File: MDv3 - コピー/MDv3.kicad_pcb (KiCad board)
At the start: 2 copper layers, 59.3 x 76.1 mm, 46 parts, among them J1 XT60PW-M, J2 XT60PW-M, J3 XT30PW-M, J4 XT30PW-M

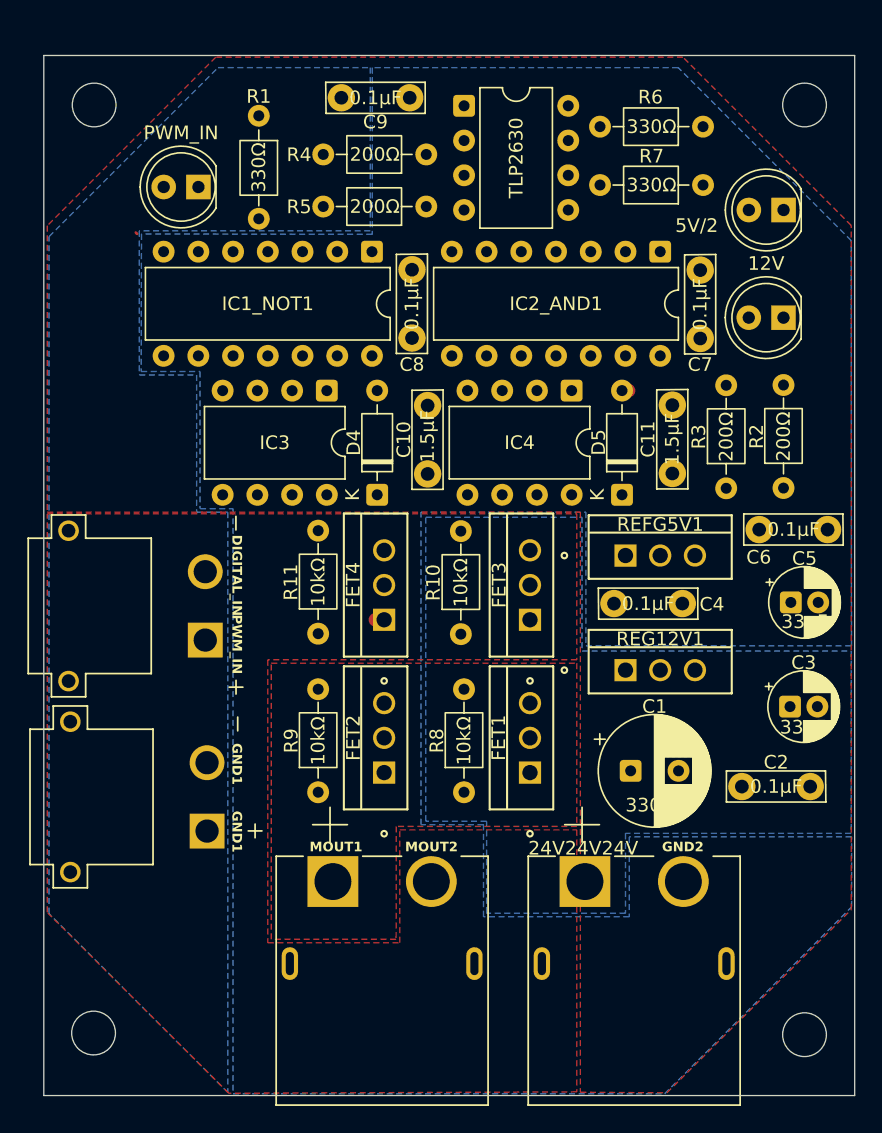
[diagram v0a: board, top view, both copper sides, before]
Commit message: 不要な塗りつぶしを削除、二層にして横向きXTにするということは基盤を大きくしてもいいということだ。
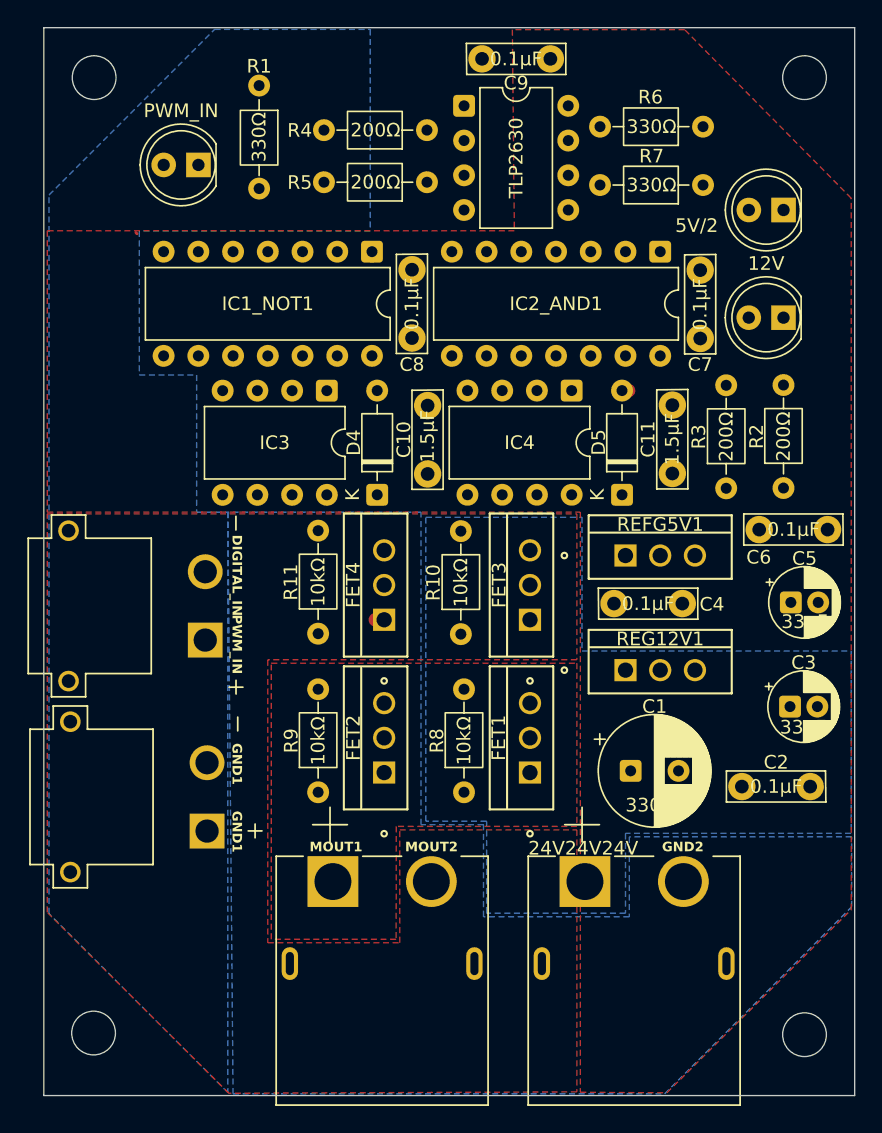
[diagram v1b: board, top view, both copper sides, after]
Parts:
- moved C9 10.7 mm to (123.4, 111.7)
- moved R1 2.21 mm to (102.1, 113.6)
- moved REF** 2.00 mm to (142.0, 113.0)
- moved REF** 2.00 mm to (90.0, 113.0)
- moved R4 1.78 mm to (114.4, 116.9)
- moved R5 1.78 mm to (114.4, 120.7)
- moved D1 1.61 mm to (97.7, 119.4)
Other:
- board size 59.3 x 76.1 mm -> 59.3 x 78.1 mm
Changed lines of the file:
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@@
 	(footprint "Library:R_Axial_DIN0207_L6.3mm_D2.5mm_P10.16mm_Horizontal_kai"
 		(layer "F.Cu")
-		(at 114.3 122.452 180)
+		(at 114.3502 120.674 180)
 		(property "Reference" "R5"
 			(at 7 -2.25 180)
@@
 	(footprint "MountingHole:MountingHole_3.2mm_M3"
 		(layer "F.Cu")
-		(at 142 115)
+		(at 142 113)
 		(descr "Mounting Hole 3.2mm, M3, no annular, generated by kicad-footprint-generator mountinghole.py")
 		(tags "mountinghole M3")
@@
 	(footprint "MountingHole:MountingHole_3.2mm_M3"
 		(layer "F.Cu")
-		(at 90.043 115)
+		(at 90.043 113)
 		(descr "Mounting Hole 3.2mm, M3, no annular, generated by kicad-footprint-generator mountinghole.py")
 		(tags "mountinghole M3")
@@
 	(footprint "Library:R_Axial_DIN0207_L6.3mm_D2.5mm_P10.16mm_Horizontal_kai"
 		(layer "F.Cu")
-		(at 102.108 115.824 -90)
+		(at 102.132 113.6148 -90)
 		(property "Reference" "R1"
 			(at 7 -2.25 270)
@@
 	(footprint "LED_THT:LED_D5.0mm"
 		(layer "F.Cu")
-		(at 97.668 121 180)
+		(at 97.668 119.385 180)
 		(descr "LED, diameter 5.0mm, 2 pins, http://cdn-reichelt.de/documents/datenblatt/A500/LL-504BC2E-009.pdf, generated by kicad-footprint-generator")
 		(tags "LED")
@@
 	(footprint "Library:C_Disc_D11.0mm_W5.0mm_P5.0mm_kai"
 		(layer "F.Cu")
-		(at 113.1295 114.5165 180)
+		(at 123.4165 111.6705 180)
 		(property "Reference" "C9"
 			(at 5 -2 180)
@@
 	(footprint "Library:R_Axial_DIN0207_L6.3mm_D2.5mm_P10.16mm_Horizontal_kai"
 		(layer "F.Cu")
-		(at 114.3 118.642 180)
+		(at 114.3502 116.864 180)
 		(property "Reference" "R4"
 			(at 7 -2.25 180)
@@
 	)
 	(gr_rect
-		(start 86.36 111.379)
+		(start 86.36 109.347)
 		(end 145.669 187.452)
 		(stroke
@@
 		(polygon
 			(pts
-				(xy 125.603 187.211026) (xy 131.930282 187.251586) (xy 145.415 173.853031) (xy 145.415 123.814)
-				(xy 133.107 111.506) (xy 98.931 111.506) (xy 86.614 123.823) (xy 86.614 144.78) (xy 125.603 144.78)
+				(xy 125.603 187.211026) (xy 131.930282 187.251586) (xy 145.415 173.853031) (xy 145.415 121.815466)
+				(xy 133.232197 109.492) (xy 120.631182 109.492) (xy 120.777 124.206) (xy 86.614 124.20018) (xy 86.614 144.78)
+				(xy 125.603 144.78)
 			)
 		)
@@
 			(pts
 				(xy 110.236 124.206) (xy 93.345 124.206) (xy 93.345 134.747) (xy 97.536 134.747) (xy 97.536 144.78)
-				(xy 99.822 144.78) (xy 99.822 187.071) (xy 99.822 187.22975) (xy 86.741 174.14875) (xy 86.741 124.634)
-				(xy 99.107 112.268) (xy 110.236 112.268)
+				(xy 99.822 144.78) (xy 99.822 187.071) (xy 99.822 187.22975) (xy 86.741 174.14875) (xy 86.741 121.586)
+				(xy 98.853 109.474) (xy 110.236 109.474)
 			)
 		)
@@
 			(pts
 				(xy 129.185597 168.529725) (xy 129.185597 174.371725) (xy 118.517597 174.371725) (xy 118.517597 167.640725)
-				(xy 113.945597 167.640725) (xy 113.945597 144.780725) (xy 126.010597 144.780725) (xy 126.010597 154.559725)
-				(xy 145.434879 154.559725) (xy 145.416101 124.916419) (xy 132.759602 112.26822) (xy 110.389597 112.268725)
-				(xy 110.389597 124.46) (xy 93.505341 124.434828) (xy 93.47872 134.493) (xy 97.79 134.493) (xy 97.79 144.526)
-				(xy 100.203 144.526344) (xy 100.203 187.324943) (xy 131.769052 187.325617) (xy 145.441597 173.653363)
-				(xy 145.441597 168.529725)
+				(xy 113.945597 167.640725) (xy 113.945597 144.780725) (xy 99.822 144.78) (xy 100.203 187.324943)
+				(xy 131.769052 187.325617) (xy 145.441597 173.653363) (xy 145.441597 168.529725)
 			)
 		)

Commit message: ようはこういうことですよね
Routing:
- net +5V/2: track 0.67 -> 126.9 mm
- net +12V: track 0.60 -> 73.8 mm
- net PWM_NOT: track 0.00 -> 26.4 mm, vias 0 -> 1
- net DIGITAL_NOT: track 0.51 -> 23.9 mm
- net Net-(D2-A): track 0.00 -> 21.9 mm
- net Net-(D4-K): track 0.01 -> 8.01 mm
- net Net-(D1-A): track 0.00 -> 7.70 mm
- net Net-(D3-A): track 0.00 -> 5.63 mm
- net Net-(R4-Pad1): track 0.00 -> 3.03 mm
- net Net-(R5-Pad1): track 0.48 -> 3.40 mm

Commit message: 一旦詰み
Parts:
- moved C10 0.64 mm to (113.8, 142.0)
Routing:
- net PWM_IN: track 0.00 -> 68.2 mm, vias 0 -> 2
- net GND1: track 0.00 -> 59.0 mm, vias 0 -> 1
- net DIGITAL_IN: track 0.13 -> 54.4 mm
- net PWM1: track 0.00 -> 33.9 mm
- net DIGITAL: track 0.00 -> 26.7 mm, vias 0 -> 2
- net MOUT2: track 0.01 -> 15.2 mm
- net MOUT1: track 0.00 -> 14.5 mm
- net GATE2: track 0.00 -> 12.4 mm, vias 0 -> 3
- net Net-(D5-K): track 0.00 -> 8.01 mm
- net Net-(D1-A): track 7.70 -> 10.8 mm
- net +12V: track 73.8 -> 76.7 mm
- net +5V/2: track 126.9 -> 125.9 mm
- net PWM_NOT: track 26.4 -> 25.5 mm, vias 1 -> 0
- net Net-(D4-K): track 8.01 -> 7.35 mm

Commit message: 無理矢理完成
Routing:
- net Net-(FET1-G): track 0.00 -> 57.4 mm, vias 0 -> 12
- net Net-(FET2-G): track 0.00 -> 33.0 mm, vias 0 -> 3
- net MOUT1: track 14.5 -> 42.3 mm, vias 0 -> 4
- net GATE1: track 0.00 -> 22.4 mm, vias 0 -> 4
- net Net-(FET3-G): track 0.00 -> 18.7 mm
- net Net-(FET4-G): track 0.63 -> 19.0 mm
- net MOUT2: track 15.2 -> 19.3 mm

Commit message: いや無理じゃね？
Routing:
- net Net-(FET1-G): track 57.4 -> 59.0 mm
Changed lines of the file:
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@@
+	)
+	(segment
+		(start 113.99813 153.97187)
+		(end 113.9952 153.9748)
+		(width 1)
+		(layer "F.Cu")
+		(net 6)
+	)
+	(segment
+		(start 112.906257 151.229374)
+		(end 113.99813 152.321247)
+		(width 1)
+		(layer "F.Cu")
+		(net 6)
 	)
 	(segment
@@
 	)
 	(segment
-		(start 113.9952 153.9748)
+		(start 112.906257 150.2156)
+		(end 112.906257 151.229374)
+		(width 1)
+		(layer "F.Cu")
+		(net 6)
+	)
+	(segment
+		(start 113.99813 152.321247)
 		(end 113.99813 153.97187)
 		(width 1)
@@
 		(net 6)
 	)
-	(segment
-		(start 113.99813 153.97187)
-		(end 113.99813 152.321247)
-		(width 1)
-		(layer "F.Cu")
-		(net 6)
-	)
-	(segment
-		(start 113.99813 152.321247)
-		(end 112.9696 151.292717)
-		(width 1)
-		(layer "F.Cu")
-		(net 6)
-	)
-	(via
-		(at 112.9696 151.292717)
+	(via
+		(at 112.906257 150.2156)
 		(size 0.6)
 		(drill 0.3)
@@
 	)
 	(segment
-		(start 112.906257 151.229374)
-		(end 112.9696 151.292717)
-		(width 0.2)
-		(layer "B.Cu")
-		(net 6)
-	)
-	(segment
 		(start 104.399 141.097)
 		(end 101.981 143.515)
@@
 	)
 	(segment
+		(start 112.906257 146.848472)
+		(end 112.906257 150.2156)
+		(width 1)
+		(layer "B.Cu")
+		(net 6)
+	)
+	(segment
 		(start 109.655 141.097)
 		(end 110.0995 140.6525)
@@
 	)
 	(segment
-		(start 112.906257 146.848472)
-		(end 112.906257 151.229374)
-		(width 1)
-		(layer "B.Cu")
-		(net 6)
-	)
-	(segment
 		(start 114.503078 140.2525)
 		(end 110.4995 140.2525)
@@
 	)
 	(segment
-		(start 104.3432 161.6456)
+		(start 104.3148 164.4396)
 		(end 104.3432 164.468)
-		(width 0.6)
+		(width 0.2)
 		(layer "F.Cu")
 		(net 13)
@@
 	)
 	(segment
+		(start 102.273 159.7152)
+		(end 102.274 159.7162)
+		(width 0.6)
+		(layer "F.Cu")
+		(net 13)
+	)
+	(segment
+		(start 102.274 159.7162)
+		(end 102.274 164.4396)
+		(width 0.6)
+		(layer "F.Cu")
+		(net 13)
+	)
+	(segment
 		(start 97.7392 141.5796)
 		(end 97.7392 144.6276)
@@
 	)
 	(segment
-		(start 103.5812 160.8836)
-		(end 104.3432 161.6456)
-		(width 0.6)
-		(layer "F.Cu")
-		(net 13)
-	)
-	(segment
 		(start 111.1504 166.624)
 		(end 113.538 166.624)
@@
 	)
 	(segment
+		(start 102.273 158.8516)
+		(end 102.273 159.7152)
+		(width 0.6)
+		(layer "F.Cu")
+		(net 13)
+	)
+	(segment
+		(start 102.274 164.4396)
+		(end 104.3148 164.4396)
+		(width 0.6)
+		(layer "F.Cu")
+		(net 13)
+	)
+	(segment
 		(start 120.482 165.268)
 		(end 121.92 163.83)
@@
 	)
 	(via
-		(at 103.5812 160.8836)
-		(size 0.6)
-		(drill 0.3)
-		(layers "F.Cu" "B.Cu")
-		(net 13)
-	)
-	(via
 		(at 95.955386 152.863014)
 		(size 0.6)
@@
 	(via
 		(at 95.9612 148.298)
+		(size 0.6)
+		(drill 0.3)
+		(layers "F.Cu" "B.Cu")
+		(net 13)
+	)
+	(via
+		(at 102.273 158.8516)
 		(size 0.6)
 		(drill 0.3)
@@
 	)
 	(segment
-		(start 95.981219 155.468019)
-		(end 101.3968 160.8836)
-		(width 0.6)
-		(layer "B.Cu")
-		(net 13)
-	)
-	(segment
 		(start 104.3432 164.468)
 		(end 104.3432 166.068)
@@
 	)
 	(segment
-		(start 95.981219 154.929283)
-		(end 95.981219 155.468019)
-		(width 0.6)
-		(layer "B.Cu")
-		(net 13)
-	)
-	(segment
-		(start 101.3968 160.8836)
-		(end 103.5812 160.8836)
+		(start 102.273 158.8516)
+		(end 99.3648 158.8516)
 		(width 0.6)
 		(layer "B.Cu")
@@
 	)
 	(segment
+		(start 99.3648 158.8516)
+		(end 95.981219 155.468019)
+		(width 0.6)
+		(layer "B.Cu")
+		(net 13)
+	)
+	(segment
 		(start 114.9956 165.268)
 		(end 117.094 165.268)
@@
 	)
 	(segment
+		(start 95.981219 155.468019)
+		(end 95.981219 154.929283)
+		(width 0.6)
+		(layer "B.Cu")
+		(net 13)
+	)
+	(segment
 		(start 95.9612 149.898)
 		(end 95.9612 152.8572)
@@
 	)
 	(segment
-		(start 101.473 146.558)
-		(end 101.473 151.003)
+		(start 100.8888 164.6428)
+		(end 101.473 165.227)
+		(width 0.6)
+		(layer "F.Cu")
+		(net 14)
+	)
+	(segment
+		(start 100.8888 155.6004)
+		(end 100.8888 164.6428)
+		(width 0.6)
+		(layer "F.Cu")
+		(net 14)
+	)
+	(segment
+		(start 100.1776 146.6088)
+		(end 100.1776 149.6568)
 		(width 0.6)
 		(layer "F.Cu")
@@
 	)
 	(segment
+		(start 100.6856 155.3972)
+		(end 100.8888 155.6004)
+		(width 0.6)
+		(layer "F.Cu")
+		(net 14)
+	)
+	(segment
 		(start 103.251 165.227)
 		(end 103.292 165.268)
@@
 		(net 14)
 	)
-	(segment
-		(start 101.473 155.067)
-		(end 101.473 165.227)
-		(width 0.6)
-		(layer "F.Cu")
-		(net 14)
-	)
-	(via
-		(at 101.473 151.003)
-		(size 0.6)
-		(drill 0.3)
-		(layers "F.Cu" "B.Cu")
-		(net 14)
-	)
-	(via
-		(at 101.473 155.067)
-		(size 0.6)
-		(drill 0.3)
-		(layers "F.Cu" "B.Cu")
-		(net 14)
-	)
-	(via
-		(at 101.473 146.558)
-		(size 0.6)
-		(drill 0.3)
-		(layers "F.Cu" "B.Cu")
+	(via
+		(at 100.1776 149.6568)
+		(size 0.6)
+		(drill 0.3)
+		(layers "F.Cu" "B.Cu")
+		(net 14)
+	)
+	(via
+		(at 100.6856 155.3972)
+		(size 0.6)
+		(drill 0.3)
+		(layers "F.Cu" "B.Cu")
+		(net 14)
+	)
+	(via
+		(at 100.1776 146.6088)
+		(size 0.6)
+		(drill 0.3)
+		(layers "F.Cu" "B.Cu")
+		(net 14)
+	)
+	(segment
+		(start 100.1776 154.8892)
+		(end 100.6856 155.3972)
+		(width 0.6)
+		(layer "B.Cu")
 		(net 14)
 	)
@@
 	)
 	(segment
-		(start 101.473 151.003)
-		(end 101.473 155.067)
-		(width 0.6)
-		(layer "B.Cu")
-		(net 14)
-	)
-	(segment
-		(start 99.441 143.515)
-		(end 101.473 145.547)
+		(start 100.1776 149.6568)
+		(end 100.1776 154.8892)
+		(width 0.6)
+		(layer "B.Cu")
+		(net 14)
+	)
+	(segment
+		(start 100.1776 144.2516)
+		(end 99.441 143.515)
+		(width 0.6)
+		(layer "B.Cu")
+		(net 14)
+	)
+	(segment
+		(start 100.1776 146.6088)
+		(end 100.1776 144.2516)
 		(width 0.6)
 		(layer "B.Cu")
@@
 		(width 0.6)
 		(layer "B.Cu")
-		(net 14)
-	)
-	(segment
-		(start 101.473 145.547)
-		(end 101.473 146.558)
-		(width 0.6)
-		(layer "B.Cu")
